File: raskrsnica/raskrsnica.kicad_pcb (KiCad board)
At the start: 2 copper layers, 40 parts, among them J1 Screw_Terminal_01x02, U1 74HC595, U2 74HC595

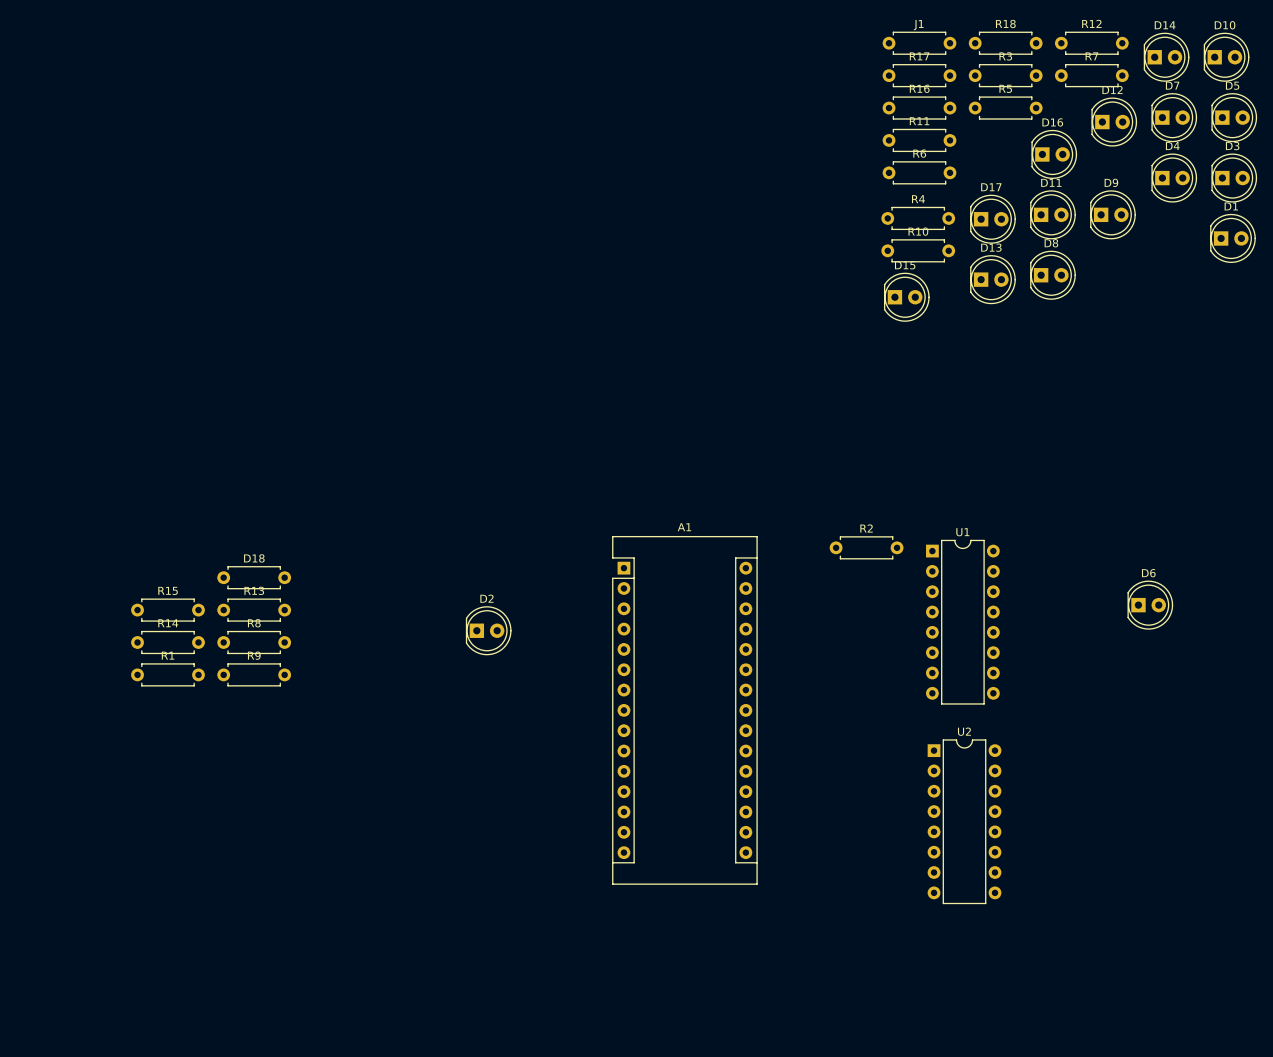
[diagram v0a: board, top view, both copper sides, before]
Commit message: Raskrsnica sa konektorima -PCB not done
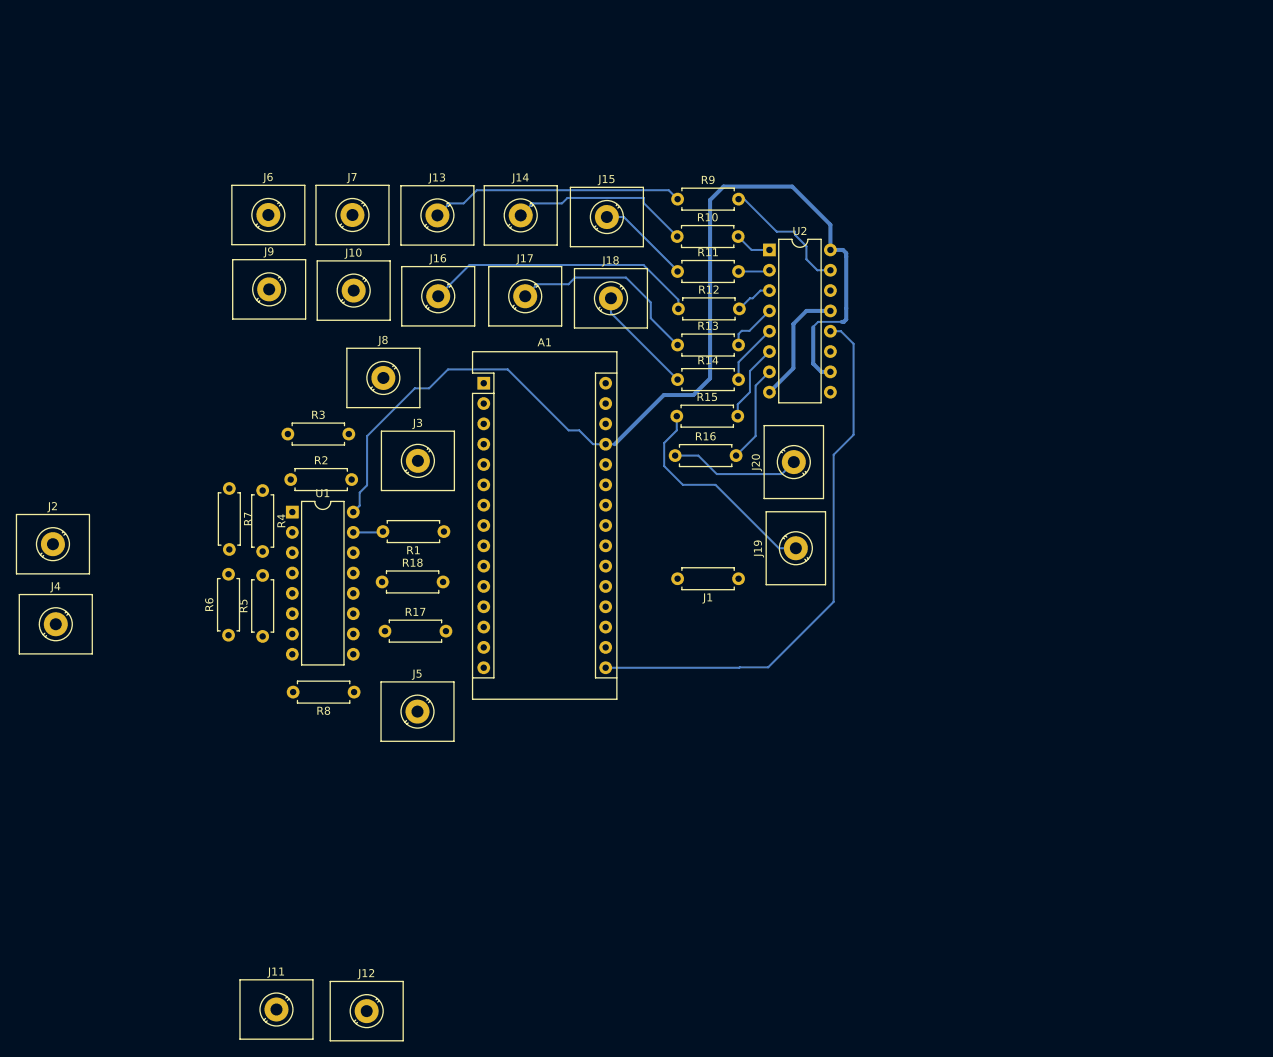
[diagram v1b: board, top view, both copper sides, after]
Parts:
- removed D1, D10, D11, D12, D13, D14, D15, D16, D17, D2, D3, D4, D5, D6, D7, D8, D9: LED, LED_THT:LED_D5.0mm_Clear
- removed D18: LED, Resistor_THT:R_Axial_DIN0207_L6.3mm_D2.5mm_P7.62mm_Horizontal
- added J10: Screw_Terminal_01x01, TerminalBlock_MetzConnect:TerminalBlock_MetzConnect_360271_1x01_Horizontal_ScrewM3.0_Boxed, F.Cu at (59.6, 58.1)
- added J11: Screw_Terminal_01x01, TerminalBlock_MetzConnect:TerminalBlock_MetzConnect_360271_1x01_Horizontal_ScrewM3.0_Boxed, F.Cu at (49.9, 147.9)
- added J13: Screw_Terminal_01x01, TerminalBlock_MetzConnect:TerminalBlock_MetzConnect_360271_1x01_Horizontal_ScrewM3.0_Boxed, F.Cu at (70.1, 48.7)
- added J14: Screw_Terminal_01x01, TerminalBlock_MetzConnect:TerminalBlock_MetzConnect_360271_1x01_Horizontal_ScrewM3.0_Boxed, F.Cu at (80.5, 48.7)
- added J15: Screw_Terminal_01x01, TerminalBlock_MetzConnect:TerminalBlock_MetzConnect_360271_1x01_Horizontal_ScrewM3.0_Boxed, F.Cu at (91.2, 48.9)
- added J16: Screw_Terminal_01x01, TerminalBlock_MetzConnect:TerminalBlock_MetzConnect_360271_1x01_Horizontal_ScrewM3.0_Boxed, F.Cu at (70.2, 58.8)
- added J17: Screw_Terminal_01x01, TerminalBlock_MetzConnect:TerminalBlock_MetzConnect_360271_1x01_Horizontal_ScrewM3.0_Boxed, F.Cu at (81.0, 58.8)
- added J18: Screw_Terminal_01x01, TerminalBlock_MetzConnect:TerminalBlock_MetzConnect_360271_1x01_Horizontal_ScrewM3.0_Boxed, F.Cu at (91.7, 59.0)
- added J19: Screw_Terminal_01x01, TerminalBlock_MetzConnect:TerminalBlock_MetzConnect_360271_1x01_Horizontal_ScrewM3.0_Boxed, F.Cu at (114.9, 90.3)
- added J2: Screw_Terminal_01x01, TerminalBlock_MetzConnect:TerminalBlock_MetzConnect_360271_1x01_Horizontal_ScrewM3.0_Boxed, F.Cu at (22.0, 89.8)
- added J20: Screw_Terminal_01x01, TerminalBlock_MetzConnect:TerminalBlock_MetzConnect_360271_1x01_Horizontal_ScrewM3.0_Boxed, F.Cu at (114.6, 79.5)
- added J3: Screw_Terminal_01x01, TerminalBlock_MetzConnect:TerminalBlock_MetzConnect_360271_1x01_Horizontal_ScrewM3.0_Boxed, F.Cu at (67.6, 79.3)
- added J4: Screw_Terminal_01x01, TerminalBlock_MetzConnect:TerminalBlock_MetzConnect_360271_1x01_Horizontal_ScrewM3.0_Boxed, F.Cu at (22.4, 99.8)
- added J5: Screw_Terminal_01x01, TerminalBlock_MetzConnect:TerminalBlock_MetzConnect_360271_1x01_Horizontal_ScrewM3.0_Boxed, F.Cu at (67.6, 110.7)
- added J6: Screw_Terminal_01x01, TerminalBlock_MetzConnect:TerminalBlock_MetzConnect_360271_1x01_Horizontal_ScrewM3.0_Boxed, F.Cu at (48.9, 48.6)
- added J7: Screw_Terminal_01x01, TerminalBlock_MetzConnect:TerminalBlock_MetzConnect_360271_1x01_Horizontal_ScrewM3.0_Boxed, F.Cu at (59.4, 48.6)
- added J8: Screw_Terminal_01x01, TerminalBlock_MetzConnect:TerminalBlock_MetzConnect_360271_1x01_Horizontal_ScrewM3.0_Boxed, F.Cu at (63.3, 69.0)
- added J9: Screw_Terminal_01x01, TerminalBlock_MetzConnect:TerminalBlock_MetzConnect_360271_1x01_Horizontal_ScrewM3.0_Boxed, F.Cu at (49.0, 57.9)
- added U2: 74HC595, Package_DIP:DIP-16_W7.62mm, F.Cu at (111.6, 53.0)
- J12: renamed from U2; value 74HC595 -> Screw_Terminal_01x01; footprint Package_DIP:DIP-16_W7.62mm -> TerminalBlock_MetzConnect:TerminalBlock_MetzConnect_360271_1x01_Horizontal_ScrewM3.0_Boxed
- moved R7 116.1 mm to (44.0, 82.8), turned to 270 degrees
- moved R5 110.9 mm to (48.2, 101.3), turned to 90 degrees
- moved R6 100.8 mm to (43.9, 101.1), turned to 90 degrees
- moved R18 100.2 mm to (63.1, 94.5)
- moved R3 96.9 mm to (51.4, 76.0)
- moved R17 93.8 mm to (63.5, 100.6)
- moved R4 85.2 mm to (48.2, 83.1), turned to 270 degrees
- moved R9 82.2 mm to (100.1, 46.6)
- moved U1 80.2 mm to (51.9, 85.8)
- moved J12 78.0 mm to (61.2, 148.1)
- moved R14 75.1 mm to (100.1, 69.2)
- moved R15 71.6 mm to (100.0, 73.8)
- moved J1 69.5 mm to (107.7, 94.1), turned to 180 degrees
- moved R2 68.7 mm to (51.7, 81.7)
- moved R13 65.7 mm to (100.1, 64.9)
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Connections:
- J12 pad 1: Net-(R10-Pad2) -> Net-(J12-Pad1)
- R8 pad 1: Net-(D10-Pad2) -> Net-(J12-Pad1)
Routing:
- net /5V: track 0.00 -> 137.1 mm
- net Net-(A1-Pad16): track 0.00 -> 68.7 mm
- net Net-(J16-Pad1): track 0.00 -> 34.6 mm
- net Net-(J13-Pad1): track 0.00 -> 31.8 mm
- net Net-(J19-Pad1): track 0.00 -> 27.6 mm
- net Net-(J17-Pad1): track 0.00 -> 24.7 mm
- net Net-(J14-Pad1): track 0.00 -> 22.8 mm
- net Net-(J20-Pad1): track 0.00 -> 16.4 mm
- net Net-(R9-Pad2): track 0.00 -> 16.4 mm
- net GND: track 0.00 -> 15.1 mm
- net Net-(J18-Pad1): track 0.00 -> 13.6 mm
- net Net-(R16-Pad2): track 0.00 -> 12.2 mm
- net Net-(J15-Pad1): track 0.00 -> 11.7 mm
- net Net-(R15-Pad2): track 0.00 -> 9.72 mm
- net Net-(R14-Pad2): track 0.00 -> 7.64 mm
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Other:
- rule pad_to_mask_clearance: 0.051 -> 0

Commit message: Layot ver 1
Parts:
- moved J6 81.3 mm to (91.0, 118.2)
- moved J7 72.6 mm to (80.7, 118.0)
- moved J11 68.4 mm to (114.0, 124.0)
- moved J9 60.8 mm to (58.6, 118.0)
- moved U1 59.7 mm to (110.2, 98.7)
- moved R7 57.3 mm to (96.1, 106.8), turned to 0 degrees
- moved J4 54.9 mm to (59.0, 58.9)
- moved R6 53.8 mm to (97.7, 102.3), turned to 0 degrees
- moved R4 52.1 mm to (99.4, 92.9), turned to 0 degrees
- moved R5 50.3 mm to (98.4, 97.4), turned to 0 degrees
- moved R3 49.7 mm to (99.5, 88.3)
- moved J8 49.6 mm to (70.0, 118.1)
- moved J10 49.4 mm to (57.5, 107.4)
- moved R2 47.7 mm to (99.4, 83.6)
- moved J2 44.9 mm to (66.7, 86.0)
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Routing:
- net Net-(A1-Pad16): track 68.7 -> 0.00 mm
- net Net-(J19-Pad1): track 27.6 -> 0.00 mm
- net Net-(J20-Pad1): track 16.4 -> 0.00 mm
- net Net-(R2-Pad2): track 0.00 -> 16.3 mm
- net Net-(R3-Pad2): track 0.00 -> 14.2 mm
- net Net-(R4-Pad2): track 0.00 -> 12.1 mm
- net Net-(R5-Pad2): track 0.00 -> 10.6 mm
- net Net-(R6-Pad2): track 0.00 -> 8.93 mm
- net Net-(R7-Pad2): track 0.00 -> 8.40 mm
- net Net-(R8-Pad2): track 0.00 -> 5.77 mm
- net Net-(R1-Pad2): track 3.75 -> 8.97 mm

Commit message: Layot ver 2
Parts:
- moved J5 5.67 mm to (102.2, 123.8)
- moved J7 5.67 mm to (81.3, 123.6)
- moved J8 5.67 mm to (70.6, 123.7)
- moved J9 5.67 mm to (59.2, 123.6)
- moved J6 5.67 mm to (91.6, 123.8)
- moved J10 3.82 mm to (56.8, 111.2)
- moved J12 3.56 mm to (68.2, 111.0)
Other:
- board outline added: 72 x 87 mm
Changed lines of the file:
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@@
   (general
     (thickness 1.6)
-    (drawings 1)
+    (drawings 4)
     (tracks 129)
     (zones 0)
@@
   )
   (module TerminalBlock_MetzConnect:TerminalBlock_MetzConnect_360271_1x01_Horizontal_ScrewM3.0_Boxed (layer F.Cu)
-    (at 68.3768 107.4928)
+    (at 68.2244 111.0488)
     (descr "single screw terminal block Metz Connect 360271, block size 9x7.3mm^2, drill diamater 1.5mm, 1 pads, pad diameter 3mm, see http://www.metz-connect.com/de/system/files/METZ_CONNECT_U_Contact_Katalog_Anschlusssysteme_fuer_Leiterplatten_DE_31_07_2017_OFF_024803.pdf?language=en page 134, script-generated using https://github.com/pointhi/kicad-footprint-generator/scripts/TerminalBlock_MetzConnect")
     (tags "THT single screw terminal block Metz Connect 360271 size 9x7.3mm^2 drill 1.5mm pad 3mm")
@@
   )
   (module TerminalBlock_MetzConnect:TerminalBlock_MetzConnect_360271_1x01_Horizontal_ScrewM3.0_Boxed (layer F.Cu)
-    (at 57.4548 107.3912)
+    (at 56.7944 111.1504)
     (descr "single screw terminal block Metz Connect 360271, block size 9x7.3mm^2, drill diamater 1.5mm, 1 pads, pad diameter 3mm, see http://www.metz-connect.com/de/system/files/METZ_CONNECT_U_Contact_Katalog_Anschlusssysteme_fuer_Leiterplatten_DE_31_07_2017_OFF_024803.pdf?language=en page 134, script-generated using https://github.com/pointhi/kicad-footprint-generator/scripts/TerminalBlock_MetzConnect")
     (tags "THT single screw terminal block Metz Connect 360271 size 9x7.3mm^2 drill 1.5mm pad 3mm")
@@
   )
   (module TerminalBlock_MetzConnect:TerminalBlock_MetzConnect_360271_1x01_Horizontal_ScrewM3.0_Boxed (layer F.Cu)
-    (at 58.5724 117.9576)
+    (at 59.182 123.5964)
     (descr "single screw terminal block Metz Connect 360271, block size 9x7.3mm^2, drill diamater 1.5mm, 1 pads, pad diameter 3mm, see http://www.metz-connect.com/de/system/files/METZ_CONNECT_U_Contact_Katalog_Anschlusssysteme_fuer_Leiterplatten_DE_31_07_2017_OFF_024803.pdf?language=en page 134, script-generated using https://github.com/pointhi/kicad-footprint-generator/scripts/TerminalBlock_MetzConnect")
     (tags "THT single screw terminal block Metz Connect 360271 size 9x7.3mm^2 drill 1.5mm pad 3mm")
@@
   )
   (module TerminalBlock_MetzConnect:TerminalBlock_MetzConnect_360271_1x01_Horizontal_ScrewM3.0_Boxed (layer F.Cu)
-    (at 70.0024 118.11)
+    (at 70.612 123.7488)
     (descr "single screw terminal block Metz Connect 360271, block size 9x7.3mm^2, drill diamater 1.5mm, 1 pads, pad diameter 3mm, see http://www.metz-connect.com/de/system/files/METZ_CONNECT_U_Contact_Katalog_Anschlusssysteme_fuer_Leiterplatten_DE_31_07_2017_OFF_024803.pdf?language=en page 134, script-generated using https://github.com/pointhi/kicad-footprint-generator/scripts/TerminalBlock_MetzConnect")
     (tags "THT single screw terminal block Metz Connect 360271 size 9x7.3mm^2 drill 1.5mm pad 3mm")
@@
   )
   (module TerminalBlock_MetzConnect:TerminalBlock_MetzConnect_360271_1x01_Horizontal_ScrewM3.0_Boxed (layer F.Cu)
-    (at 80.6704 118.0084)
+    (at 81.28 123.6472)
     (descr "single screw terminal block Metz Connect 360271, block size 9x7.3mm^2, drill diamater 1.5mm, 1 pads, pad diameter 3mm, see http://www.metz-connect.com/de/system/files/METZ_CONNECT_U_Contact_Katalog_Anschlusssysteme_fuer_Leiterplatten_DE_31_07_2017_OFF_024803.pdf?language=en page 134, script-generated using https://github.com/pointhi/kicad-footprint-generator/scripts/TerminalBlock_MetzConnect")
     (tags "THT single screw terminal block Metz Connect 360271 size 9x7.3mm^2 drill 1.5mm pad 3mm")
@@
   )
   (module TerminalBlock_MetzConnect:TerminalBlock_MetzConnect_360271_1x01_Horizontal_ScrewM3.0_Boxed (layer F.Cu)
-    (at 91.0336 118.1608)
+    (at 91.6432 123.7996)
     (descr "single screw terminal block Metz Connect 360271, block size 9x7.3mm^2, drill diamater 1.5mm, 1 pads, pad diameter 3mm, see http://www.metz-connect.com/de/system/files/METZ_CONNECT_U_Contact_Katalog_Anschlusssysteme_fuer_Leiterplatten_DE_31_07_2017_OFF_024803.pdf?language=en page 134, script-generated using https://github.com/pointhi/kicad-footprint-generator/scripts/TerminalBlock_MetzConnect")
     (tags "THT single screw terminal block Metz Connect 360271 size 9x7.3mm^2 drill 1.5mm pad 3mm")
@@
   )
   (module TerminalBlock_MetzConnect:TerminalBlock_MetzConnect_360271_1x01_Horizontal_ScrewM3.0_Boxed (layer F.Cu)
-    (at 101.5492 118.1608)
+    (at 102.1588 123.7996)
     (descr "single screw terminal block Metz Connect 360271, block size 9x7.3mm^2, drill diamater 1.5mm, 1 pads, pad diameter 3mm, see http://www.metz-connect.com/de/system/files/METZ_CONNECT_U_Contact_Katalog_Anschlusssysteme_fuer_Leiterplatten_DE_31_07_2017_OFF_024803.pdf?language=en page 134, script-generated using https://github.com/pointhi/kicad-footprint-generator/scripts/TerminalBlock_MetzConnect")
     (tags "THT single screw terminal block Metz Connect 360271 size 9x7.3mm^2 drill 1.5mm pad 3mm")
@@
     )
   )
-  (gr_line (start 124 43) (end 124 122) (layer Edge.Cuts) (width 0.254))
+  (gr_line (start 52 130) (end 124 130) (layer Edge.Cuts) (width 0.254))
+  (gr_line (start 52 43) (end 52 130) (layer Edge.Cuts) (width 0.254))
+  (gr_line (start 124 43) (end 52 43) (layer Edge.Cuts) (width 0.254))
+  (gr_line (start 124 43) (end 124 130) (layer Edge.Cuts) (width 0.254))
   (segment (start 116.1796 60.6044) (end 114.554 62.23) (width 0.5) (layer B.Cu) (net 5))
   (segment (start 119.1768 60.6044) (end 116.1796 60.6044) (width 0.5) (layer B.Cu) (net 5))

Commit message: Raskrsnica layout finished
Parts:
- moved J12 36.9 mm to (102.1, 125.8)
- moved J10 28.5 mm to (81.2, 125.8)
- moved J11 22.4 mm to (91.7, 125.8)
- moved J8 12.4 mm to (81.2, 117.3)
- moved J6 12.3 mm to (102.1, 117.3)
- moved J7 12.2 mm to (91.7, 117.3)
- moved J9 10.8 mm to (70.0, 124.5)
- moved J5 10.2 mm to (112.3, 123.0)
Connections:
- A1 pad 29: GND -> Net-(A1-Pad29)
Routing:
- net Net-(A1-Pad15): track 0.00 -> 161.9 mm
- net Net-(A1-Pad16): track 0.00 -> 160.8 mm
- net GND: track 15.1 -> 149.3 mm, vias 0 -> 1
- net Net-(A1-Pad14): track 0.00 -> 95.2 mm
- net Net-(A1-Pad13): track 0.00 -> 80.8 mm
- net Net-(J12-Pad1): track 0.00 -> 56.3 mm
- net Net-(J11-Pad1): track 0.00 -> 48.9 mm
- net Net-(J9-Pad1): track 0.00 -> 47.3 mm
- net Net-(J10-Pad1): track 0.00 -> 46.9 mm
- net Net-(J8-Pad1): track 0.00 -> 42.7 mm
- net Net-(J6-Pad1): track 0.00 -> 41.1 mm
- net Net-(J7-Pad1): track 0.00 -> 38.8 mm
- net Net-(J5-Pad1): track 0.00 -> 33.9 mm
- net Net-(J19-Pad1): track 0.00 -> 30.3 mm
- net /5V: track 137.5 -> 107.8 mm, vias 0 -> 3
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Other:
- board text added: "5V"
- board text added: "Emrah Skender Aladin Jazvin prof. Anel Husakovic"
- board text added: "GND"
- board text added: "Srednja mjesovita skola Mladost Zenica Festival rada Buzim "Pametna raskrsnica""
- board text added: "april, 2019"
